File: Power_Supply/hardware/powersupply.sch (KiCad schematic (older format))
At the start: 84 parts, among them J1 1x2, J101 USB_B_Micro, J102 Conn_01x03_Male, J103 Default_Jumper, J104 Default_Jumper, J2 1x2, Q1 IRF9Z24NPBF, SW1 KMR2, SW2 joystick-K1-1506DN-01, SW3 KMR2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

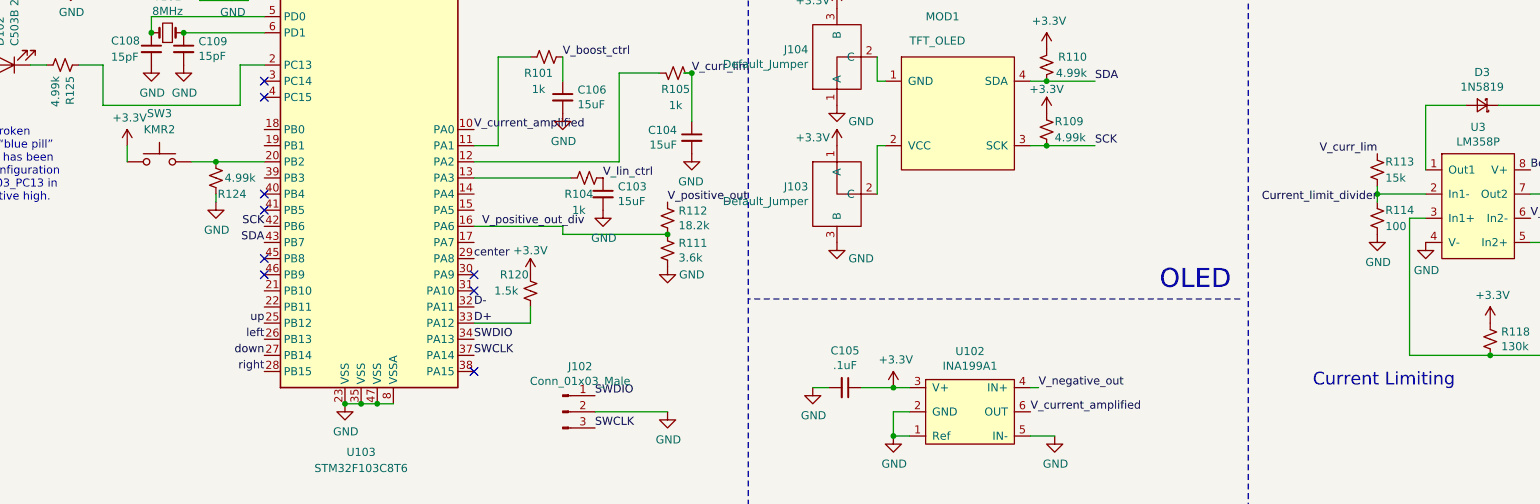
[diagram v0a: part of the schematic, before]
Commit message: Moved current sense amplifier away from switching components.
Moved current sense amplifier away from switching components.
Moved boost converter filtering components nearer to the output of the
boost converter.
Moved P-MOSFET down a bit so it’s farther away from the joystick.
Firmware: V_current_amplified moved to PB0
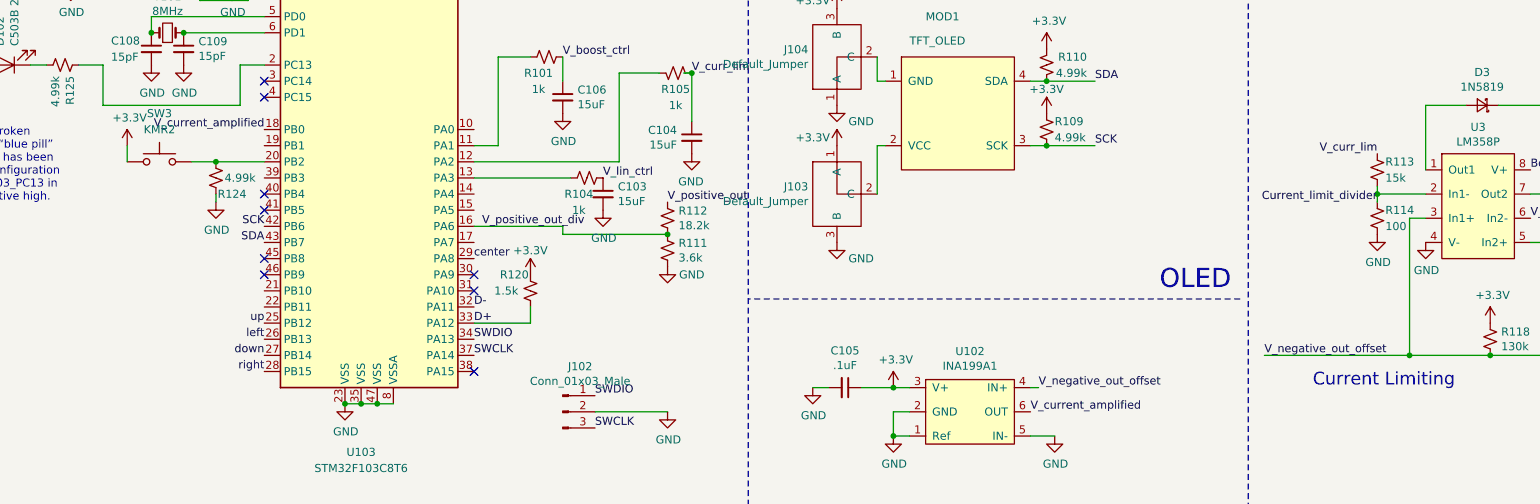
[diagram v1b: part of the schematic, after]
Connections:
- net V_current_amplified: now also U103.18 (PB0); no longer U103.10 (PA0)
- net V_negative_out: no longer U102.4 (IN+)
- net V_negative_out_offset: now reaches R117.1, R118.2, U3.3 (In1+)
- net V_negative_out_offset: now also U102.4 (IN+)
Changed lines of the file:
@@
 	9900 5300 10500 5300
 Text Label 5650 5500 0    50   ~ 0
-V_negative_out
+V_negative_out_offset
 Wire Wire Line
 	9000 5300 9150 5300
@@
 Wire Wire Line
 	3450 3550 3500 3550
-Text Label 2150 3900 0    50   ~ 0
-V_current_amplified
 Text Label 2950 4200 0    50   ~ 0
 V_lin_ctrl
@@
 Text Label 2200 4500 0    50   ~ 0
 V_positive_out_div
+Connection ~ 7950 5300
+Text Label 7050 5300 0    50   ~ 0
+V_negative_out_offset
+Wire Wire Line
+	7050 5300 7950 5300
+Text Label 850  3900 2    50   ~ 0
+V_current_amplified
 $EndSCHEMATC

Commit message: fixed labels
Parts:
- renumbered D3 to D1, R3 to R1, U3 to U1
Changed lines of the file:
@@
 EESchema Schematic File Version 4
-EELAYER 30 0
+LIBS:powersupply-cache
+EELAYER 29 0
 EELAYER END
 $Descr A4 11693 8268
@@
 NoConn ~ 25200 10700
 $Comp
-L powersupply:LM358P U3
+L powersupply:LM358P U1
 U 1 1 5D4A8FA5
 P 8400 4000
-F 0 "U3" H 8375 4115 50  0000 C CNN
+F 0 "U1" H 8375 4115 50  0000 C CNN
 F 1 "LM358P" H 8375 4024 50  0000 C CNN
 F 2 "Package_DIP:DIP-8_W7.62mm" H 8400 4000 50  0001 C CNN
@@
 $EndComp
 $Comp
-L Device:D_Schottky_Small D3
+L Device:D_Schottky_Small D1
 U 1 1 5D4E566E
 P 8400 3750
-F 0 "D3" H 8400 3545 50  0000 C CNN
+F 0 "D1" H 8400 3545 50  0000 C CNN
 F 1 "1N5819" H 8400 3636 50  0000 C CNN
 F 2 "Diode_THT:D_DO-41_SOD81_P7.62mm_Horizontal" V 8400 3750 50  0001 C CNN
@@
 Connection ~ 4750 5500
 $Comp
-L Device:R_Small_US R3
+L Device:R_Small_US R1
 U 1 1 5D45B2AA
 P 7950 1500
-F 0 "R3" H 8018 1546 50  0000 L CNN
+F 0 "R1" H 8018 1546 50  0000 L CNN
 F 1 "0.3 1/4W" H 8018 1455 50  0000 L CNN
 F 2 "Resistor_THT:R_Axial_DIN0207_L6.3mm_D2.5mm_P10.16mm_Horizontal" H 7950 1500 50  0001 C CNN

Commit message: some layout changes
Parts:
- C116: renamed from C3; footprint Capacitor_THT:C_Rect_L4.0mm_W2.5mm_P2.50mm -> Capacitor_SMD:C_0805_2012Metric
- R126: renamed from R1; footprint Resistor_THT:R_Axial_DIN0207_L6.3mm_D2.5mm_P10.16mm_Horizontal -> Resistor_SMD:R_0805_2012Metric
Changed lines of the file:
@@
 Connection ~ 4750 5500
 $Comp
-L Device:R_Small_US R1
+L Device:R_Small_US R126
 U 1 1 5D45B2AA
 P 7950 1500
-F 0 "R1" H 8018 1546 50  0000 L CNN
+F 0 "R126" H 8018 1546 50  0000 L CNN
 F 1 "0.3 1/4W" H 8018 1455 50  0000 L CNN
-F 2 "Resistor_THT:R_Axial_DIN0207_L6.3mm_D2.5mm_P10.16mm_Horizontal" H 7950 1500 50  0001 C CNN
+F 2 "Resistor_SMD:R_0805_2012Metric" H 7950 1500 50  0001 C CNN
 F 3 "~" H 7950 1500 50  0001 C CNN
 	1    7950 1500
@@
 $EndComp
 $Comp
-L Device:C_Small C3
+L Device:C_Small C116
 U 1 1 5D4C7F8E
 P 9850 1750
-F 0 "C3" H 9700 1800 50  0000 L CNN
+F 0 "C116" H 9700 1800 50  0000 L CNN
 F 1 "270pF" H 9450 1700 50  0000 L CNN
-F 2 "Capacitor_THT:C_Rect_L4.0mm_W2.5mm_P2.50mm" H 9850 1750 50  0001 C CNN
+F 2 "Capacitor_SMD:C_0805_2012Metric" H 9850 1750 50  0001 C CNN
 F 3 "~" H 9850 1750 50  0001 C CNN
 	1    9850 1750
